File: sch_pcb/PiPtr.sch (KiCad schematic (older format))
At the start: 67 parts, among them J101 GLOBAL LINK 1 LEFT, J102 GLOBAL LINK 1 RIGHT, J104 GLOBAL LINK 2 LEFT, J106 GLOBAL LINK 2 RIGHT, J107 RASPBERRY_PI, J111 FP_PIXEL, J112 AM2302, J113 I2C1_5V, J114 I2C0_3v3, J117 OLED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

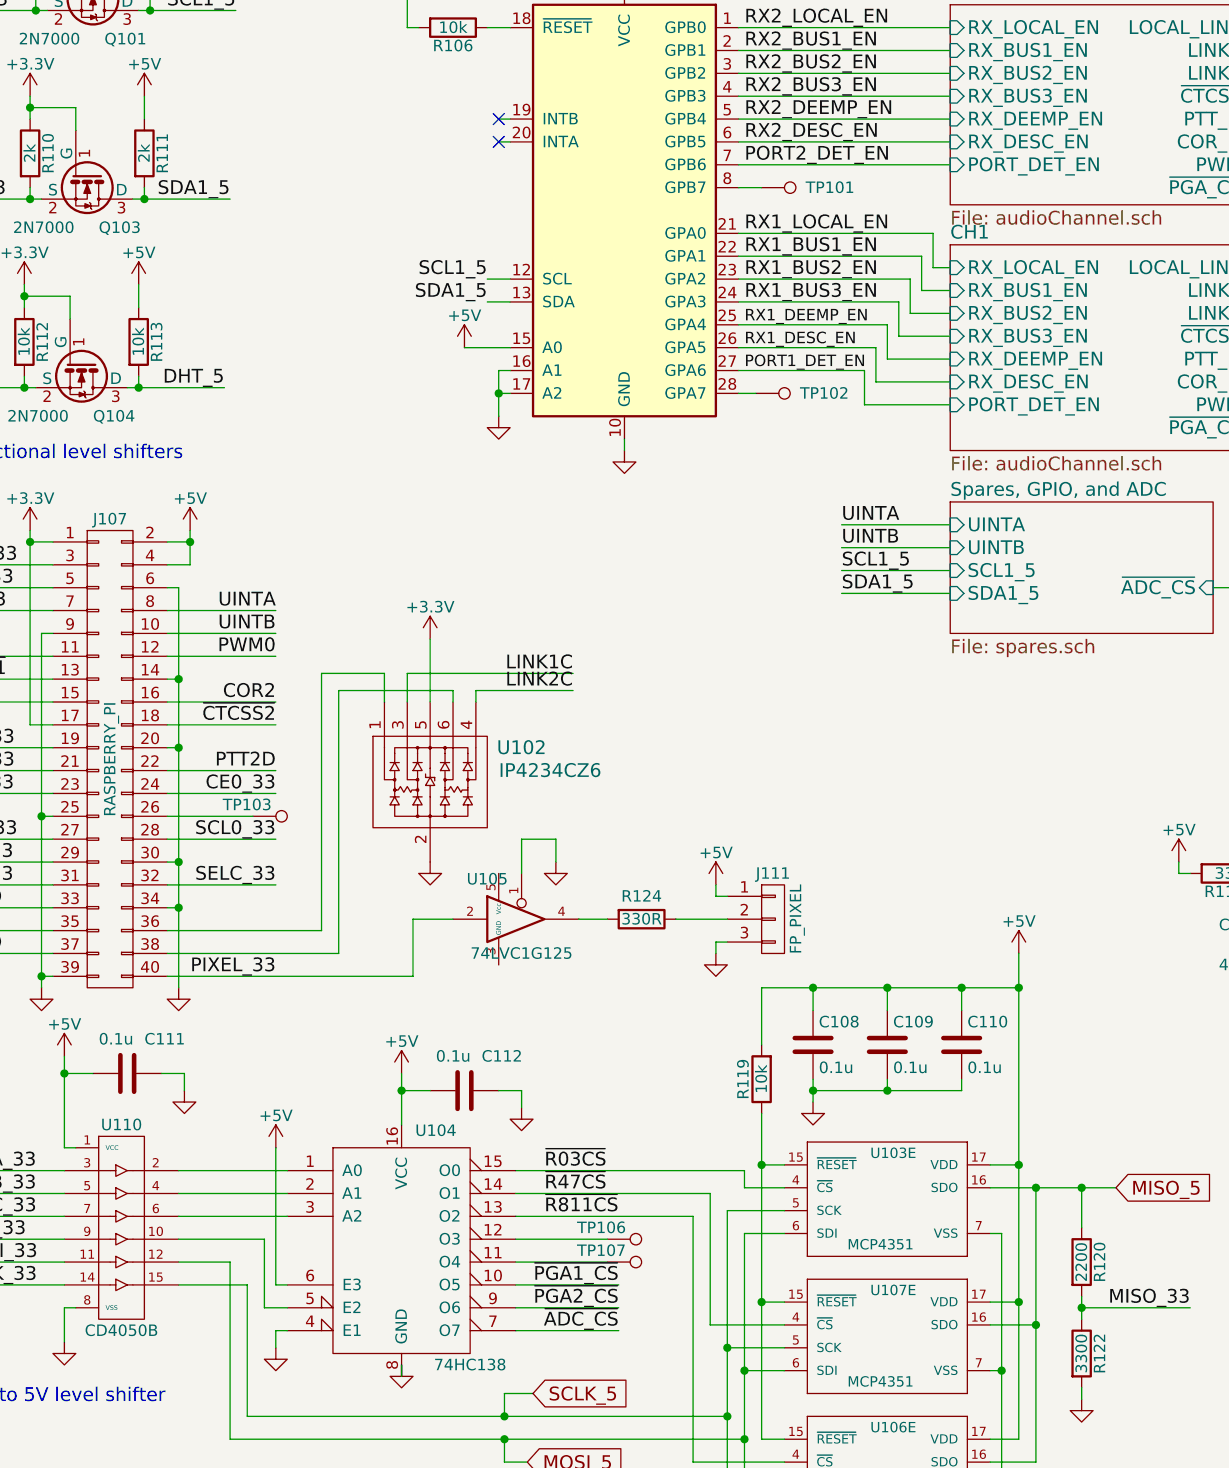
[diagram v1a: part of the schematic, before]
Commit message: Add files via upload
Changed  user_adc connector to 2x7 (14-pin is a lot more common than 12-pin)
Changed user_gpio connector to 2 2x8 connectors.  1x20 takes too much linear space
First pass layout on the two audio channels.  Right now, board is 4-layer, 100x150mm.  May be able to knock down the 150mm dimension 
The link and soundcard connectors fit in a row across the front edge.
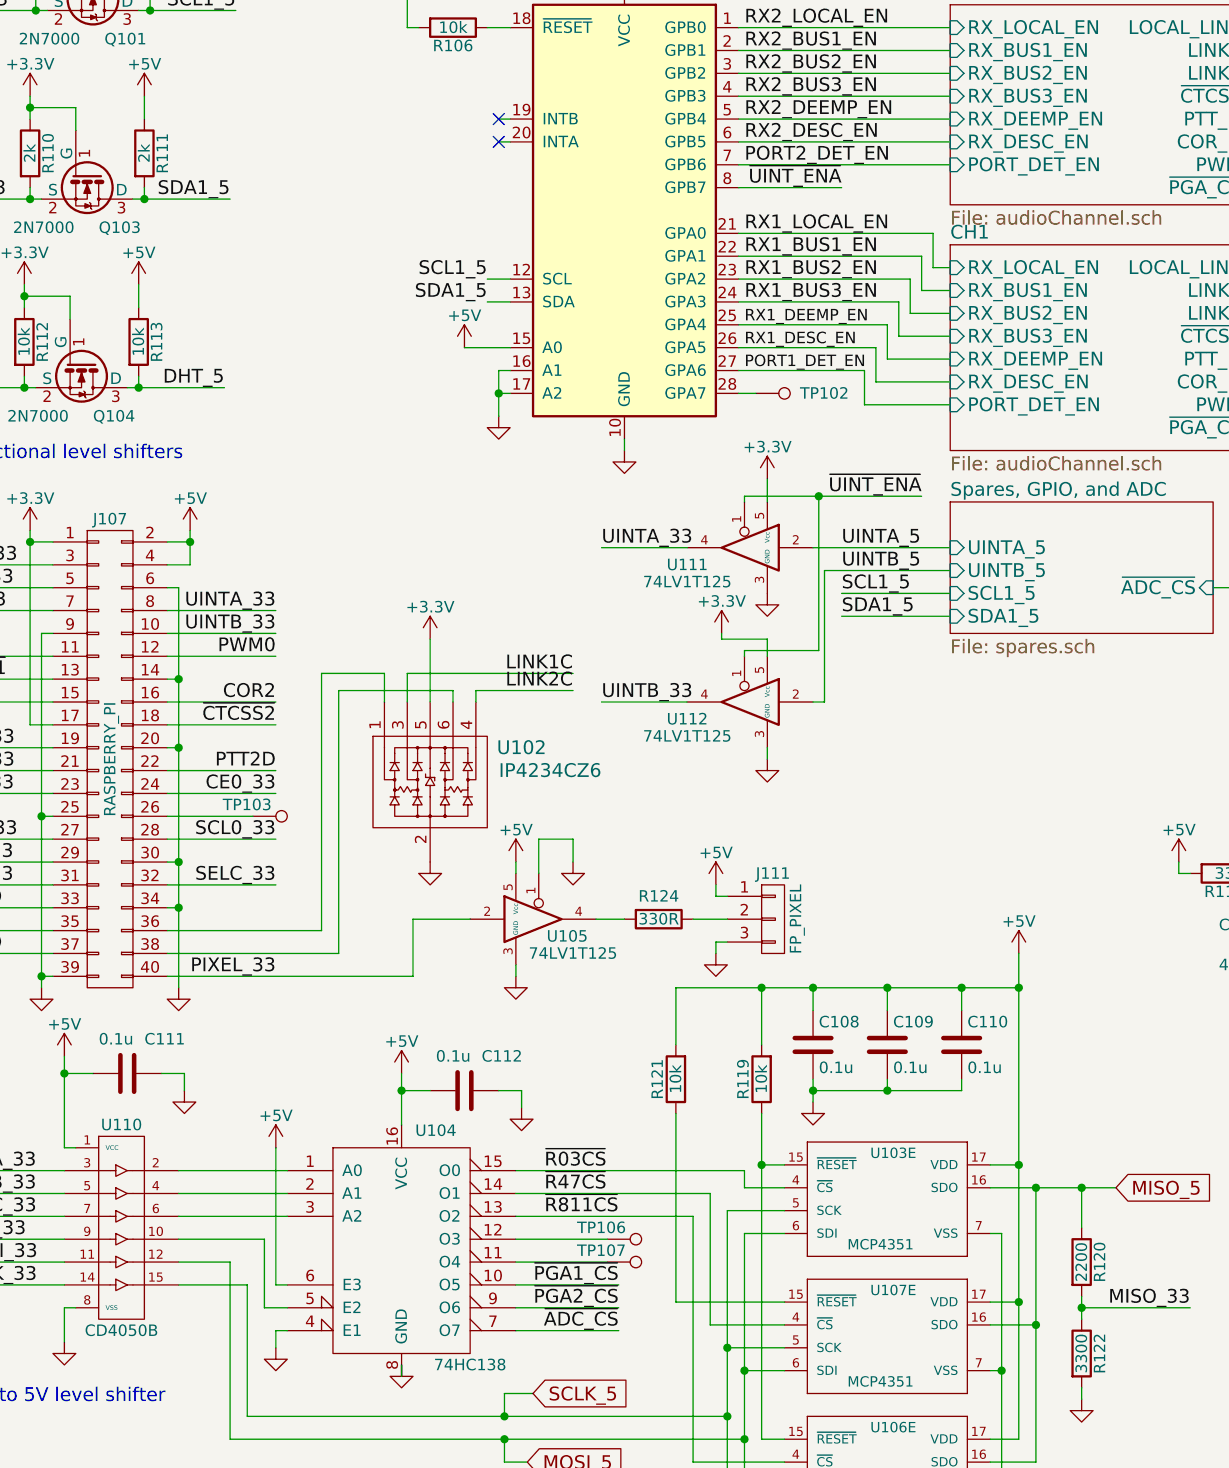
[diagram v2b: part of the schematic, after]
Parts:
- removed TP101: TESTPOINT, lib:Wire_28AWG, symbol TESTPOINT
- added R121: 10k, lib:smd0603, symbol R
- added U111, U112: 74LV1T125, lib:SOT23-5, symbol 74LVC1G125
- U105: value 74LVC1G125 -> 74LV1T125
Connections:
- net +3V3: now also U111.5 (Vcc), U112.5 (Vcc)
- net +5V: now also U105.5 (Vcc), R121.2
- net GND: now also U105.3 (GND), U111.3 (GND), U112.3 (GND)
- net ~UINT_ENA: now reaches U101.8 (GPB7)
- net ~UINT_ENA: now also U111.1, U112.1
- net at R119.1, U103.15 (~RESET), U106.15 (~RESET): no longer U107.15 (~RESET)
- net UINTA renamed UINTA_33
- net UINTA_33: now also U111.4
- net UINTB renamed UINTB_33
- net UINTB_33: now also U112.4
- new net: R121.1, U107.15 (~RESET)
- new net UINTA_5: U111.2
- new net UINTB_5: U112.2
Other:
- moved on the sheet: R124, U105
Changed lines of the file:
@@
 F0 "Spares, GPIO, and ADC" 60
 F1 "spares.sch" 60
-F2 "UINTA" I L 5050 3400 60
-F3 "UINTB" I L 5050 3500 60
-F4 "SCL1_5" I L 5050 3600 60
-F5 "SDA1_5" I L 5050 3700 60
-F6 "~ADC_CS" I R 6200 3675 60
+F2 "SCL1_5" I L 5050 3700 60
+F3 "SDA1_5" I L 5050 3800 60
+F4 "~ADC_CS" I R 6200 3675 60
+F5 "UINTA_5" I L 5050 3500 60
+F6 "UINTB_5" I L 5050 3600 60
 $EndSheet
 Text Label 8825 775  0    60   ~ 0
@@
 Connection ~ 5625 6825
 Wire Wire Line
-	3850 5125 4075 5125
+	3925 5125 4075 5125
 Wire Wire Line
 	4075 5025 4025 5025
@@
 	4125 1825 5050 1825
 Wire Wire Line
-	4125 1925 4225 1925
+	4125 1925 4575 1925
 Wire Wire Line
 	4125 2125 4975 2125
@@
 	3150 6725 3600 6725
 Text Label 2100 3775 2    60   ~ 0
-UINTA
+UINTA_33
 Text Label 2100 3875 2    60   ~ 0
-UINTB
+UINTB_33
 $Comp
 L C C110
@@
 	4225 5675 4225 5425
 Wire Wire Line
-	4225 5425 5350 5425
+	3850 5425 5350 5425
 Wire Wire Line
 	5100 5425 5100 5525
@@
 	4225 7400 4325 7400
 Wire Wire Line
-	4325 6800 4225 6800
-Connection ~ 4225 6800
-Wire Wire Line
-	4325 6200 4225 6200
+	4225 6200 4325 6200
 Connection ~ 4225 6200
 Wire Wire Line
@@
 	6200 3675 6625 3675
 Wire Wire Line
-	5050 3400 4575 3400
-Wire Wire Line
-	5050 3500 4575 3500
-Wire Wire Line
-	5050 3600 4575 3600
+	5050 3500 4450 3500
+Wire Wire Line
+	4500 3600 5050 3600
 Wire Wire Line
 	5050 3700 4575 3700
-Text Label 4575 3400 0    60   ~ 0
-UINTA
+Wire Wire Line
+	5050 3800 4575 3800
 Text Label 4575 3500 0    60   ~ 0
-UINTB
+UINTA_5
+Text Label 4575 3600 0    60   ~ 0
+UINTB_5
+Text Label 4575 3800 0    60   ~ 0
+SDA1_5
 Text Label 4575 3700 0    60   ~ 0
-SDA1_5
-Text Label 4575 3600 0    60   ~ 0
 SCL1_5
 Text GLabel 3225 7200 2    60   Input ~ 0
@@
 L R R124
 U 1 1 595B58A6
-P 3700 5125
-F 0 "R124" V 3600 5125 50  0000 C CNN
-F 1 "330R" V 3700 5125 50  0000 C CNN
-F 2 "lib:smd0603" V 3630 5125 50  0001 C CNN
-F 3 "" H 3700 5125 50  0001 C CNN
-	1    3700 5125
+P 3775 5125
+F 0 "R124" V 3675 5125 50  0000 C CNN
+F 1 "330R" V 3775 5125 50  0000 C CNN
+F 2 "lib:smd0603" V 3705 5125 50  0001 C CNN
+F 3 "" H 3775 5125 50  0001 C CNN
+	1    3775 5125
 	0    1    1    0
 $EndComp
 Wire Wire Line
-	3425 5125 3550 5125
+	3500 5125 3625 5125
 $Comp
 L IP4234CZ6_USB_ESD_PROTECTOR U102
@@
 $EndComp
 $Comp
-L TESTPOINT TP101
-U 1 1 595DADA4
-P 4225 1925
-F 0 "TP101" H 4525 1925 50  0000 C CNN
-F 1 "TESTPOINT" H 4625 2000 60  0001 C CNN
-F 2 "lib:Wire_28AWG" H 4225 1925 60  0001 C CNN
-F 3 "" H 4225 1925 60  0000 C CNN
-	1    4225 1925
-	1    0    0    -1
-$EndComp
-$Comp
 L TESTPOINT TP103
 U 1 1 595DBEF8
@@
 L 74LVC1G125 U105
 U 1 1 595B04C3
-P 3175 5125
-F 0 "U105" H 3025 5300 50  0000 C CNN
-F 1 "74LVC1G125" H 3175 4975 50  0000 C CNN
-F 2 "lib:SOT23-5" H 3175 5125 50  0001 C CNN
-F 3 "" H 3175 5125 50  0001 C CNN
-	1    3175 5125
+P 3250 5125
+F 0 "U105" H 3375 5050 50  0000 C CNN
+F 1 "74LV1T125" H 3400 4975 50  0000 C CNN
+F 2 "lib:SOT23-5" H 3250 5125 50  0001 C CNN
+F 3 "" H 3250 5125 50  0001 C CNN
+	1    3250 5125
 	1    0    0    -1
 $EndComp
@@
 L GND #PWR052
 U 1 1 595B3661
-P 3325 4875
-F 0 "#PWR052" H 3325 4625 50  0001 C CNN
-F 1 "GND" H 3325 4725 50  0001 C CNN
-F 2 "" H 3325 4875 50  0001 C CNN
-F 3 "" H 3325 4875 50  0001 C CNN
-	1    3325 4875
-	1    0    0    -1
-$EndComp
-Wire Wire Line
-	3175 4925 3175 4775
-Wire Wire Line
-	3175 4775 3325 4775
-Wire Wire Line
-	3325 4775 3325 4875
+P 3400 4875
+F 0 "#PWR052" H 3400 4625 50  0001 C CNN
+F 1 "GND" H 3400 4725 50  0001 C CNN
+F 2 "" H 3400 4875 50  0001 C CNN
+F 3 "" H 3400 4875 50  0001 C CNN
+	1    3400 4875
+	1    0    0    -1
+$EndComp
+Wire Wire Line
+	3250 4925 3250 4775
+Wire Wire Line
+	3250 4775 3400 4775
+Wire Wire Line
+	3400 4775 3400 4875
 $Comp
 L CD4050B_1piece U110
@@
 	2700 5375 2700 5125
 Wire Wire Line
-	2700 5125 2875 5125
+	2700 5125 2950 5125
+Text Label 4575 1925 2    60   ~ 0
+~UINT_ENA
+$Comp
+L GND #PWR055
+U 1 1 5962607B
+P 3150 5375
+F 0 "#PWR055" H 3150 5125 50  0001 C CNN
+F 1 "GND" H 3150 5225 50  0001 C CNN
+F 2 "" H 3150 5375 50  0001 C CNN
+F 3 "" H 3150 5375 50  0001 C CNN
+	1    3150 5375
+	1    0    0    -1
+$EndComp
+$Comp
+L +5V #PWR056
+U 1 1 596264CA
+P 3150 4875
+F 0 "#PWR056" H 3150 4725 50  0001 C CNN
+F 1 "+5V" H 3150 5015 50  0000 C CNN
+F 2 "" H 3150 4875 50  0001 C CNN
+F 3 "" H 3150 4875 50  0001 C CNN
+	1    3150 4875
+	1    0    0    -1
+$EndComp
+Wire Wire Line
+	3150 4875 3150 4925
+Wire Wire Line
+	3150 5325 3150 5375
+$Comp
+L 74LVC1G125 U111
+U 1 1 59628CF4
+P 4150 3500
+F 0 "U111" H 4400 3425 50  0000 C CNN
+F 1 "74LV1T125" H 4400 3350 50  0000 C CNN
+F 2 "lib:SOT23-5" H 4150 3500 50  0001 C CNN
+F 3 "" H 4150 3500 50  0001 C CNN
+	1    4150 3500
+	-1   0    0    -1
+$EndComp
+$Comp
+L 74LVC1G125 U112
+U 1 1 596298A1
+P 4150 4175
+F 0 "U112" H 4400 4100 50  0000 C CNN
+F 1 "74LV1T125" H 4400 4025 50  0000 C CNN
+F 2 "lib:SOT23-5" H 4150 4175 50  0001 C CNN
+F 3 "" H 4150 4175 50  0001 C CNN
+	1    4150 4175
+	-1   0    0    -1
+$EndComp
+Text Label 3525 3500 0    60   ~ 0
+UINTA_33
+Text Label 3525 4175 0    60   ~ 0
+UINTB_33
+Wire Wire Line
+	3525 3500 3900 3500
+Wire Wire Line
+	3900 4175 3525 4175
+Wire Wire Line
+	4500 3600 4500 4175
+Wire Wire Line
+	4500 4175 4450 4175
+Wire Wire Line
+	4250 3300 4250 3200
+Wire Wire Line
+	4250 3900 4250 3975
+Wire Wire Line
+	4250 4375 4250 4425
+Wire Wire Line
+	4150 3975 4150 3950
+Wire Wire Line
+	4150 3950 4475 3950
+Wire Wire Line
+	4475 3950 4475 3275
+Wire Wire Line
+	4150 3275 4925 3275
+Wire Wire Line
+	4150 3275 4150 3300
+$Comp
+L GND #PWR057
+U 1 1 59632375
+P 4250 4425
+F 0 "#PWR057" H 4250 4175 50  0001 C CNN
+F 1 "GND" H 4250 4275 50  0001 C CNN
+F 2 "" H 4250 4425 50  0001 C CNN
+F 3 "" H 4250 4425 50  0001 C CNN
+	1    4250 4425
+	1    0    0    -1
+$EndComp
+$Comp
+L GND #PWR058
+U 1 1 596359C1
+P 4250 3700
+F 0 "#PWR058" H 4250 3450 50  0001 C CNN
+F 1 "GND" H 4250 3550 50  0001 C CNN
+F 2 "" H 4250 3700 50  0001 C CNN
+F 3 "" H 4250 3700 50  0001 C CNN
+	1    4250 3700
+	1    0    0    -1
+$EndComp
+$Comp
+L +3.3V #PWR059
+U 1 1 596373BE
+P 4250 3200
+F 0 "#PWR059" H 4250 3050 50  0001 C CNN
+F 1 "+3.3V" H 4250 3340 50  0000 C CNN
+F 2 "" H 4250 3200 50  0001 C CNN
+F 3 "" H 4250 3200 50  0001 C CNN
+	1    4250 3200
+	1    0    0    -1
+$EndComp
+$Comp
+L +3.3V #PWR060
+U 1 1 59638398
+P 4050 3875
+F 0 "#PWR060" H 4050 3725 50  0001 C CNN
+F 1 "+3.3V" H 4050 4015 50  0000 C CNN
+F 2 "" H 4050 3875 50  0001 C CNN
+F 3 "" H 4050 3875 50  0001 C CNN
+	1    4050 3875
+	1    0    0    -1
+$EndComp
+Wire Wire Line
+	4050 3875 4050 3900
+Wire Wire Line
+	4050 3900 4250 3900
+Connection ~ 4475 3275
+Text Label 4925 3275 2    60   ~ 0
+~UINT_ENA
+$Comp
+L R R121
+U 1 1 5962A262
+P 3850 5825
+F 0 "R121" V 3930 5825 50  0000 C CNN
+F 1 "10k" V 3850 5825 50  0000 C CNN
+F 2 "lib:smd0603" V 3780 5825 50  0001 C CNN
+F 3 "" H 3850 5825 50  0001 C CNN
+	1    3850 5825
+	-1   0    0    1
+$EndComp
+Wire Wire Line
+	3850 5675 3850 5425
+Connection ~ 4225 5425
+Wire Wire Line
+	3850 5975 3850 6800
+Wire Wire Line
+	3850 6800 4325 6800
 $EndSCHEMATC

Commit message: Add files via upload
Reversed ends on all pots so up increases level
Added outline and mounting holes to RasPi footprint so we can see how big it really is
Moved parts away from one of the RasPi mounting holes so we can use all 4 of them
More routing - finished user GPIO and ADC, SPI chipselect decoder
Still to do: level shifters, RasPi connections and spares
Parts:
- J107: footprint lib:PIN_ARRAY_20X2 -> lib:RaspberryPi2x20
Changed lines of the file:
@@
 F 0 "J107" H 1375 5475 50  0000 C CNN
 F 1 "RASPBERRY_PI" V 1375 4425 50  0000 C CNN
-F 2 "lib:PIN_ARRAY_20X2" H 1375 3475 50  0001 C CNN
+F 2 "lib:RaspberryPi2x20" H 1375 3475 50  0001 C CNN
 F 3 "" H 1375 3475 50  0001 C CNN
 	1    1375 4425
